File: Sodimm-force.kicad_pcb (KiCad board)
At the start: 8 copper layers, 67.6 x 25.4 mm, 186 parts, among them J1 SODIMM-200_Split, J2 HDMI_C_1.4, J3 Micro_SD_Card_Det2, J4 USB_C_Receptacle_USB2.0_16P, J5 USB_C_Receptacle_USB2.0_16P, Q1 2N7002, SW1 SW_Push, SW2 SW_Push, SW3 SW_Push, SW4 SW_Push, U1 SPX3819M5-L, U2 SPX3819M5-L, U3 SPI-EEPROM, Y1 X322524MKB4SI

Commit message: Кучка исправлений, переместил SD карту, дисплей, в целом компоновка чуть другая Небольшие исправления в схеме 🤠
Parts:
- C55, C56, C57, C58, C59, C60, C64, C65, C66, C67, C68, C69, C70, C71, C72, C73, C74, C75, C76, C77, C78, C79, C80, C81, C82, C83, C84, C85, C86, C87, C88, DD2, DD3, DD4, DD5, L1, L2, L3, L4: moved to B.Cu
- J3: moved to F.Cu
- moved C55 89.9 mm to (81.1, 139.9), turned to 180 degrees
- moved C56 89.9 mm to (81.1, 141.9), turned to 180 degrees
- moved C57 89.9 mm to (81.1, 143.8), turned to 180 degrees
- moved C58 89.9 mm to (84.0, 132.0), turned to 180 degrees
- moved C59 89.9 mm to (84.0, 134.0), turned to 180 degrees
- moved C60 89.9 mm to (84.0, 136.0), turned to 180 degrees
- moved C64 62.9 mm to (134.2, 143.9), turned to 180 degrees
- moved C78 62.1 mm to (143.7, 140.8), turned to -90 degrees
- moved C72 61.2 mm to (137.1, 143.9)
- moved C74 60.2 mm to (142.0, 143.8)
- moved C85 59.2 mm to (132.3, 144.3), turned to 180 degrees
- moved C80 57.3 mm to (144.0, 138.9)
- moved C65 57.0 mm to (133.3, 139.6), turned to 180 degrees
- moved C73 56.1 mm to (142.4, 136.4), turned to 180 degrees
- moved C79 56.0 mm to (140.5, 137.7), turned to 90 degrees
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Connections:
- net HDMIO_TX_CEC_PORT renamed HDMI0_TX_CEC_PORT
- net HDMIO_TX_SDA_PORT renamed HDMI0_TX_SDA_PORT
- net USB0-DM renamed USB0-DN
- net USB1-DM renamed USB1-DN
- net USB3-DM renamed USB3-DN
- DD1 pad K19: USB2-DM -> USB2-DN
- J2 pad 8: HTXOP -> HTX0P
- J2 pad 9: HTXON -> HTX0N
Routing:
- net HTX2P: track 0.00 -> 23.7 mm
- net HTX0P: track 0.00 -> 23.3 mm, vias 0 -> 2
- net HTX1P: track 0.00 -> 22.9 mm
- net HTX2N: track 0.00 -> 22.8 mm
- net HTX1N: track 0.00 -> 21.9 mm, vias 0 -> 2
- net HTXCP: track 0.00 -> 21.3 mm
- net HTXCN: track 0.00 -> 20.9 mm, vias 0 -> 2
- net HTX0N: track 0.00 -> 19.5 mm
- net USB1-DN: track 0.00 -> 16.7 mm
- net USB0-DN: track 0.00 -> 16.6 mm
- net USB1-DP: track 0.00 -> 16.6 mm
- net USB0-DP: track 0.00 -> 14.4 mm, vias 0 -> 2
- net VCC-DRAM: track 51.7 -> 54.6 mm, vias 29 -> 33
- net AVCC: track 5.62 -> 7.40 mm, vias 7 -> 14
- net PI10: track 0.00 -> 1.38 mm, vias 0 -> 1
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
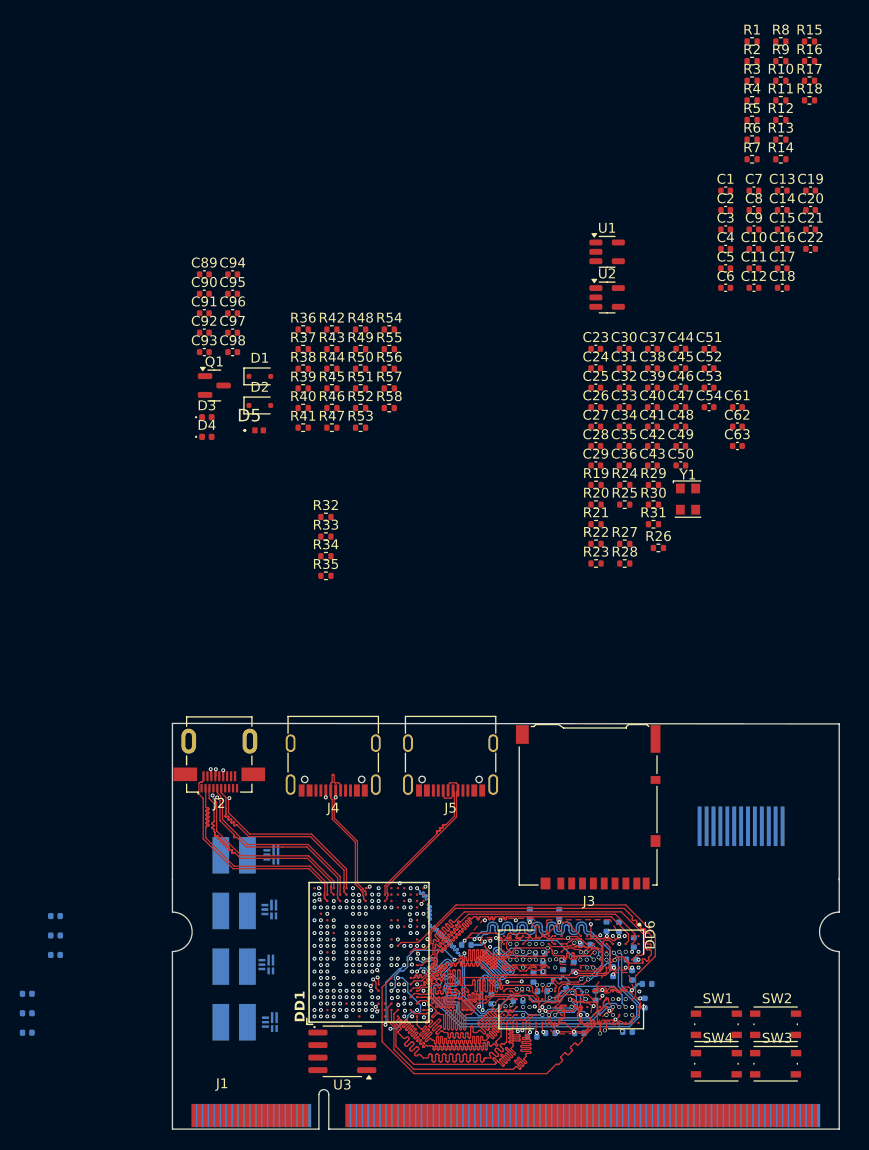
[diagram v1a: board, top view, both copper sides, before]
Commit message: Навёл красоту, убрал подтяжку для питания что скопировал с реф дизайна ( у меня не умные DC-DC ) + компоновка decoupling кондёров и быстрой обвязки чипа
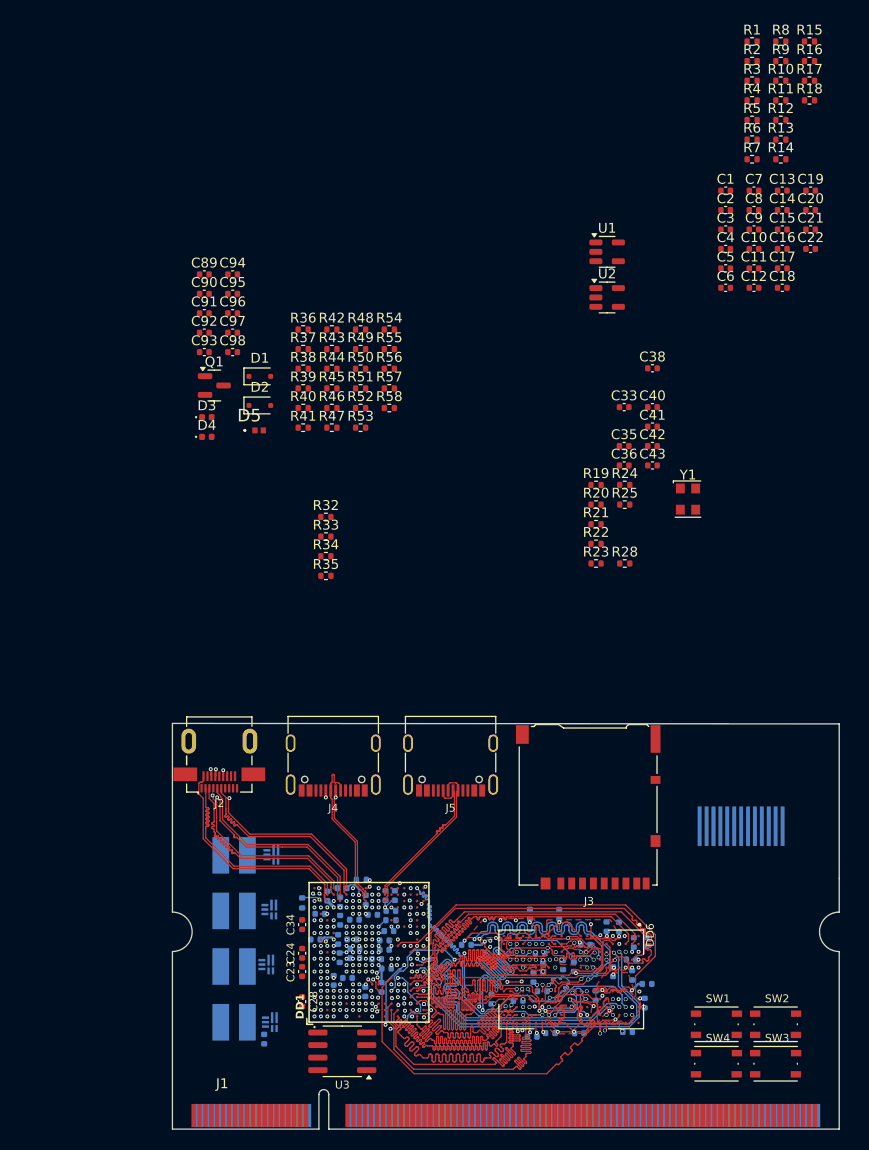
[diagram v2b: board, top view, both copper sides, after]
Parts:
- removed C31: 1nF, Capacitor_SMD:C_0402_1005Metric
- removed R26: 10K, Resistor_SMD:R_0402_1005Metric
- removed R27: 100R, Resistor_SMD:R_0402_1005Metric
- C25, C26, C27, C29, C30, C32, C37, C39, C44, C45, C46, C47, C48, C49, C50, C51, C52, C53, C54, C61, C62, C63, R29, R30, R31: moved to B.Cu
- moved C51 83.3 mm to (105.2, 144.5), turned to -90 degrees
- moved C23 69.8 mm to (109.0, 137.7), turned to 90 degrees
- moved C62 69.5 mm to (112.2, 138.6), turned to -90 degrees
- moved C44 69.2 mm to (114.3, 135.3)
- moved C45 68.3 mm to (114.3, 136.3)
- moved C61 67.5 mm to (112.7, 134.4), turned to 90 degrees
- moved C46 67.1 mm to (110.3, 134.4), turned to 180 degrees
- moved C24 66.4 mm to (109.0, 135.8), turned to 90 degrees
- moved C52 66.0 mm to (111.5, 130.0), turned to 90 degrees
- moved C47 65.7 mm to (112.8, 136.2), turned to -90 degrees
- moved C48 65.3 mm to (113.6, 138.3), turned to 180 degrees
- moved C30 64.7 mm to (112.8, 132.4), turned to -90 degrees
- moved C28 63.7 mm to (109.0, 140.7), turned to -90 degrees
- moved C37 63.0 mm to (115.5, 130.4), turned to 90 degrees
- moved C54 62.6 mm to (112.8, 130.6), turned to 90 degrees
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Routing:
- net AVCC: track 7.40 -> 11.3 mm
- net LRADC: track 0.00 -> 3.77 mm, vias 1 -> 2
- net VCC-IO: track 0.00 -> 2.00 mm
- net EPHY-RTX: track 0.00 -> 1.85 mm
- net DXLDO-OUT: track 0.00 -> 1.74 mm
- net VCC-DRAM: track 54.6 -> 56.0 mm
- net Net-(DD1C-SZQ): track 0.00 -> 1.01 mm
- net AC-AVCC: track 0.00 -> 0.94 mm
- net VDD-GPU: track 0.00 -> 0.73 mm
- net PI16: track 0.00 -> 0.67 mm
- net PH10/IR_RX: vias 1 -> 0

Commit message: Проведены все линии данных, осталось лишь сделать полигонами питание и шелкографию исправить :)
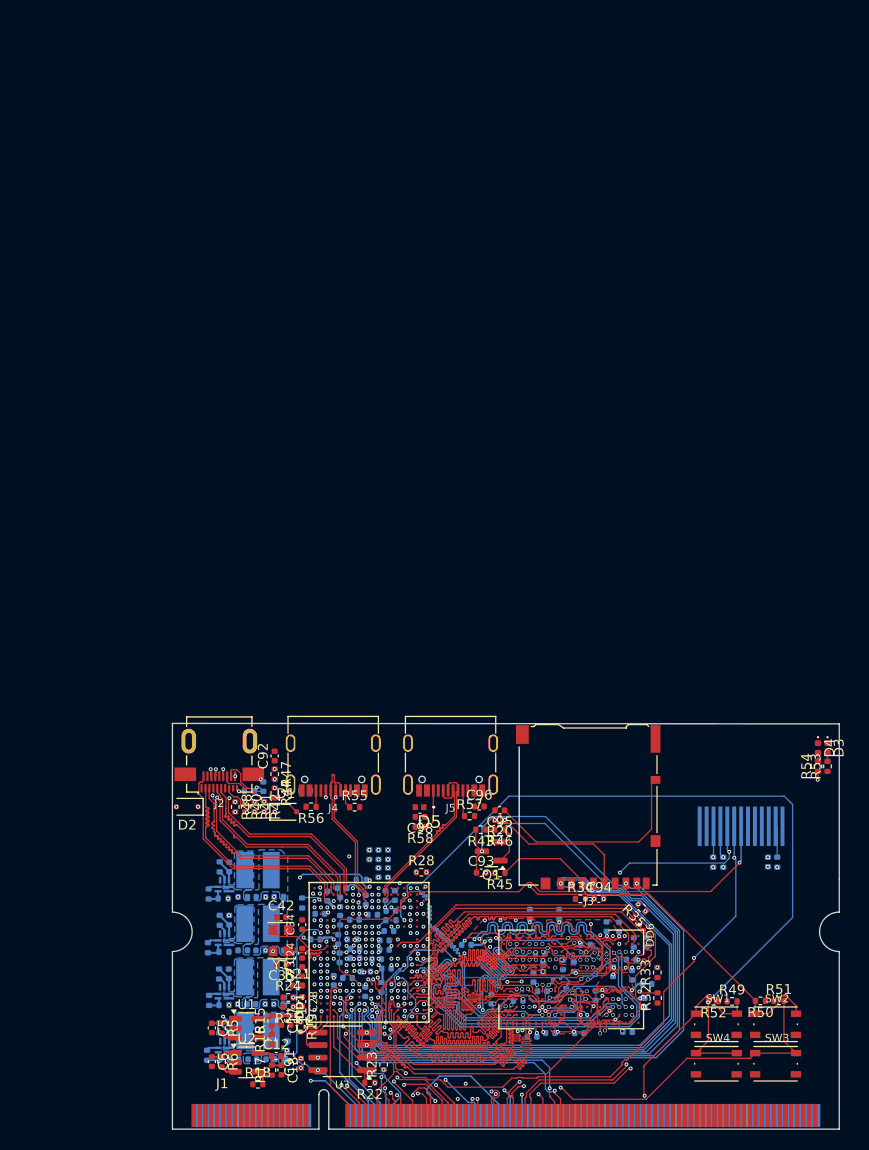
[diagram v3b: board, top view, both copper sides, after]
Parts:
- C1, C10, C13, C14, C15, C16, C19, C2, C20, C21, C22, C3, C33, C36, C38, C4, C40, C41, C43, C7, C8, C89, C9, C90, C97, R1, R10, R11, R12, R13, R14, R2, R3, R36, R37, R38, R39, R4, R7, R8, R9: moved to B.Cu
- moved R8 117.6 mm to (101.2, 146.6), turned to 180 degrees
- moved R18 114.3 mm to (104.5, 149.1)
- moved R17 114.2 mm to (105.9, 147.7), turned to 90 degrees
- moved R1 113.7 mm to (100.6, 143.4), turned to 90 degrees
- moved R15 113.2 mm to (105.9, 142.6), turned to 90 degrees
- moved R16 113.2 mm to (105.9, 144.5), turned to 90 degrees
- moved R9 111.5 mm to (99.6, 140.6), turned to 90 degrees
- moved R10 109.4 mm to (101.1, 141.1), turned to 180 degrees
- moved R6 107.9 mm to (100.8, 146.8), turned to -90 degrees
- moved R2 107.2 mm to (100.6, 137.9), turned to 90 degrees
- moved R5 106.6 mm to (100.8, 143.4), turned to -90 degrees
- moved R7 106.3 mm to (99.4, 146.1), turned to 90 degrees
- moved C19 104.2 mm to (104.9, 146.6)
- moved R11 103.7 mm to (99.5, 135.2), turned to 90 degrees
- moved C13 101.7 mm to (106.7, 146.5), turned to 180 degrees
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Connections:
- J1 pad 51: P15 -> PI15
- J1 pad 89: USB2-DM -> USB2-DN
- R54 pad 1: STATUS-:ED -> STATUS-LED
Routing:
- net PI10: track 1.38 -> 95.1 mm, vias 1 -> 3
- net SPI1_CLK: track 0.00 -> 86.0 mm, vias 1 -> 4
- net STATUS-LED: track 0.00 -> 82.1 mm, vias 1 -> 3
- net SPI1_MOSI: track 0.00 -> 82.1 mm, vias 1 -> 3
- net EPHY-TXP: track 0.00 -> 81.1 mm, vias 1 -> 2
- net EPHY-TXN: track 0.00 -> 79.2 mm, vias 1 -> 2
- net SDC0-DET: track 0.00 -> 78.7 mm, vias 1 -> 2
- net LINEOUTL: track 0.00 -> 77.3 mm, vias 1 -> 3
- net LINEOUTR: track 0.00 -> 77.1 mm, vias 1 -> 2
- net EPHY-RXP: track 0.00 -> 75.9 mm, vias 1 -> 2
- net EPHY-RXN: track 0.00 -> 74.1 mm, vias 1 -> 2
- net PI15: track 0.00 -> 73.9 mm, vias 1 -> 4
- net USB2-DN: track 0.00 -> 73.7 mm, vias 1 -> 2
- net USB2-DP: track 0.00 -> 73.5 mm, vias 1 -> 2
- net Net-(DD1A-PF2): track 0.00 -> 67.4 mm, vias 1 -> 2
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- added copper zone on B.Cu, net DCDCE
- added copper zone on B.Cu, net Net-(DD2-LX)
- added copper zone on B.Cu, net Net-(DD3-LX)
- added copper zone on B.Cu, net Net-(DD4-LX)
- added copper zone on B.Cu, net Net-(DD5-LX)
- added copper zone on B.Cu, net VCC-DRAM
- added copper zone on B.Cu, net VDD-CPU
- added copper zone on B.Cu, net VDD-GPU
